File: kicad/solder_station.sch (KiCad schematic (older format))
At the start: 31 parts, among them IC1 ATMEGA328-P, P1 CONN_01X05, P2 CONN_01X02, P3 GX16-8 Plug, P4 UART, Q1 2N7000, Q2 IRF4905, SW1 SPST, U1 LM2596_module, U2 AD8572, U3 EC11, Y1 16MHz

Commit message: [Kicad] Update Schematics. Use local labels.
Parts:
- removed P3: GX16-8 Plug, symbol CONN_01X08
- removed SW1: SPST, symbol SPST
- added D1, D2: D, Diodes_ThroughHole:Diode_DO-35_SOD27_Horizontal_RM10, symbol D
- added P3: Standby, Socket_Strips:Socket_Strip_Straight_1x01, symbol CONN_01X01
- added R10, R11: 1MΩ, Resistors_ThroughHole:Resistor_Horizontal_RM10mm, symbol R
- P1: footprint Pin_Headers:Pin_Header_Straight_1x05 -> Terminal_Blocks:TerminalBlock_Pheonix_MPT-2.54mm_5pol
- P4: footprint Pin_Headers:Pin_Header_Straight_1x03 -> Pin_Headers:Pin_Header_Straight_1x04
- Q2: symbol Q_NMOS_SGD -> Q_PMOS_SGD
- R4: value 1kΩ -> 6.7kΩ
- U3: footprint Buttons_Switches_ThroughHole:KSA_Tactile_SPST -> Pin_Headers:Pin_Header_Straight_1x05
- Y1: footprint Crystals:Crystal_HC51-U_Vertical -> Crystals:Crystal_HC49-U_Vertical
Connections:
- net labels added: Heater_PWM, Temp_sense, Tip
- net labels removed: Button_standby, Heater, RESET, Temp_sens
- wire segments 120 -> 116
- no-connect marks 11 -> 8
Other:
- note added: "Can also use a single Zener diode"
- note added: "Pin 3 and 5 are shorted by connector"
- note removed: "Extern am Addon"
- note removed: "Not part of pcb"
- moved on the sheet: C6, R4

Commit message: [Kicad] Fix bug in schematics (VGS too high). Still not sure if it is okay this way.
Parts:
- added R12: 1kΩ, Resistors_ThroughHole:Resistor_Horizontal_RM10mm, symbol R
- P1: footprint Terminal_Blocks:TerminalBlock_Pheonix_MPT-2.54mm_5pol -> Terminal_Blocks:TerminalBlock_Pheonix_PT-3.5mm_5pol
- P2: footprint Terminal_Blocks:TerminalBlock_Pheonix_MKDS1.5-2pol -> Terminal_Blocks:TerminalBlock_Pheonix_PT-3.5mm_2pol
- P3: footprint Socket_Strips:Socket_Strip_Straight_1x01 -> Pin_Headers:Pin_Header_Straight_1x01
- R5: value 10kΩ -> 1kΩ
- Y1: footprint Crystals:Crystal_HC49-U_Vertical -> Crystals:HC-49V
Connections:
- net GND: now also R12.2; no longer Q1.3 (S)
- new net: Q1.3 (S), R12.1
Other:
- moved on the sheet: R3
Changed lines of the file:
@@
 L GND #PWR06
 U 1 1 566AFDB2
-P 8300 3500
-F 0 "#PWR06" H 8300 3250 50  0001 C CNN
-F 1 "GND" H 8300 3350 50  0000 C CNN
-F 2 "" H 8300 3500 60  0000 C CNN
-F 3 "" H 8300 3500 60  0000 C CNN
-	1    8300 3500
+P 8300 3950
+F 0 "#PWR06" H 8300 3700 50  0001 C CNN
+F 1 "GND" H 8300 3800 50  0000 C CNN
+F 2 "" H 8300 3950 60  0000 C CNN
+F 3 "" H 8300 3950 60  0000 C CNN
+	1    8300 3950
 	1    0    0    -1
 $EndComp
@@
 L R R3
 U 1 1 566AFE19
-P 8100 3400
-F 0 "R3" V 8180 3400 50  0000 C CNN
-F 1 "10kΩ" V 8100 3400 50  0000 C CNN
-F 2 "Resistors_ThroughHole:Resistor_Horizontal_RM10mm" V 8030 3400 30  0001 C CNN
-F 3 "" H 8100 3400 30  0000 C CNN
-	1    8100 3400
+P 8100 3700
+F 0 "R3" V 8180 3700 50  0000 C CNN
+F 1 "10kΩ" V 8100 3700 50  0000 C CNN
+F 2 "Resistors_ThroughHole:Resistor_Horizontal_RM10mm" V 8030 3700 30  0001 C CNN
+F 3 "" H 8100 3700 30  0000 C CNN
+	1    8100 3700
 	0    -1   -1   0
 $EndComp
@@
 P 8300 1950
 F 0 "R5" V 8380 1950 50  0000 C CNN
-F 1 "10kΩ" V 8300 1950 50  0000 C CNN
+F 1 "1kΩ" V 8300 1950 50  0000 C CNN
 F 2 "Resistors_ThroughHole:Resistor_Horizontal_RM10mm" V 8230 1950 30  0001 C CNN
 F 3 "" H 8300 1950 30  0000 C CNN
@@
 F 0 "P2" H 7600 1350 50  0000 C CNN
 F 1 "CONN_01X02" V 7700 1200 50  0000 C CNN
-F 2 "Terminal_Blocks:TerminalBlock_Pheonix_MKDS1.5-2pol" H 7600 1200 60  0001 C CNN
+F 2 "Terminal_Blocks:TerminalBlock_Pheonix_PT-3.5mm_2pol" H 7600 1200 60  0001 C CNN
 F 3 "" H 7600 1200 60  0000 C CNN
 	1    7600 1200
@@
 F 0 "P1" H 10500 1000 50  0000 C CNN
 F 1 "CONN_01X05" V 10600 700 50  0000 C CNN
-F 2 "Terminal_Blocks:TerminalBlock_Pheonix_MPT-2.54mm_5pol" H 10500 700 60  0001 C CNN
+F 2 "Terminal_Blocks:TerminalBlock_Pheonix_PT-3.5mm_5pol" H 10500 700 60  0001 C CNN
 F 3 "" H 10500 700 60  0000 C CNN
 	1    10500 700
@@
 F 0 "Y1" V 5800 3400 50  0000 C CNN
 F 1 "16MHz" H 5800 3100 50  0000 C CNN
-F 2 "Crystals:Crystal_HC49-U_Vertical" H 5800 3250 60  0001 C CNN
+F 2 "Crystals:HC-49V" H 5800 3250 60  0001 C CNN
 F 3 "" H 5800 3250 60  0000 C CNN
 	1    5800 3250
@@
 F 0 "P3" H 6050 3900 50  0000 C CNN
 F 1 "Standby" V 6150 3800 50  0000 C CNN
-F 2 "Socket_Strips:Socket_Strip_Straight_1x01" H 6050 3800 60  0001 C CNN
+F 2 "Pin_Headers:Pin_Header_Straight_1x01" H 6050 3800 60  0001 C CNN
 F 3 "" H 6050 3800 60  0000 C CNN
 	1    6050 3800
@@
 	7800 3050 8000 3050
 Wire Wire Line
-	8300 3250 8300 3500
-Wire Wire Line
-	7950 3400 7950 3050
+	7950 3050 7950 3700
 Connection ~ 7950 3050
-Wire Wire Line
-	8250 3400 8300 3400
-Connection ~ 8300 3400
 Wire Wire Line
 	9100 1550 9100 2050
@@
 Text Label 7050 4900 0    60   ~ 0
 Heater+
+$Comp
+L R R12
+U 1 1 56A90FE1
+P 8300 3450
+F 0 "R12" V 8380 3450 50  0000 C CNN
+F 1 "1kΩ" V 8300 3450 50  0000 C CNN
+F 2 "Resistors_ThroughHole:Resistor_Horizontal_RM10mm" V 8230 3450 30  0001 C CNN
+F 3 "" H 8300 3450 30  0000 C CNN
+	1    8300 3450
+	1    0    0    -1
+$EndComp
+Wire Wire Line
+	8300 3300 8300 3250
+Wire Wire Line
+	8300 3600 8300 3950
+Wire Wire Line
+	8250 3700 8300 3700
+Connection ~ 8300 3700
 $EndSCHEMATC

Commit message: [Kicad] Update schematics. Using ad8551.
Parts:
- added C9: CP, Capacitors_ThroughHole:C_Radial_D5_L11_P2.5, symbol CP
- Q2: symbol Q_PMOS_SGD -> Q_PMOS_GDS
- R1: value 100kΩ -> 10kΩ
- R10: value 1MΩ -> 300kΩ
- R6: value 100Ω -> 1kΩ
- R7: value 50kΩ -> 100kΩ
- U2: value AD8572 -> AD8551; symbol LM358 -> TL071
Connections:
- net +24V: now also C9.1
- net AVcc: now also U2.7 (V+); no longer U2.8 (V+)
- net Button_push: now also IC1.16 ((PCINT2/OC1B/~SS~)PB2); no longer IC1.17 ((PCINT3/OC2A/MOSI)PB3)
- net GND: now also Q1.1 (D), C9.2; no longer R12.2
- net Heater+: now also Q2.2 (D); no longer Q2.1 (S)
- net Rotary_B: now also IC1.17 ((PCINT3/OC2A/MOSI)PB3); no longer IC1.18 ((PCINT4/MISO)PB4)
- net at Q1.3 (S): now also R12.2; no longer R12.1
- net at R7.1, R8.2: now also U2.6; no longer U2.1
- new net: Q2.1 (G), R12.1, R5.2
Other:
- note removed: "Can also use a single Zener diode"
- note removed: "Wert muss noch ermittelt werden"
- moved on the sheet: P2, R12
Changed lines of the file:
@@
 P 5900 4350
 F 0 "R1" V 6000 4400 50  0000 C CNN
-F 1 "100kΩ" V 5800 4350 50  0000 C CNN
+F 1 "10kΩ" V 5800 4350 50  0000 C CNN
 F 2 "Resistors_ThroughHole:Resistor_Horizontal_RM10mm" V 5830 4350 30  0001 C CNN
 F 3 "" H 5900 4350 30  0000 C CNN
@@
 	1    0    0    -1
 $EndComp
-NoConn ~ 4950 2850
 $Comp
 L Q_NMOS_DGS Q1
@@
 F 3 "" H 8200 3050 60  0000 C CNN
 	1    8200 3050
-	1    0    0    -1
+	1    0    0    1
 $EndComp
 $Comp
@@
 $EndComp
 $Comp
-L Q_PMOS_SGD Q2
+L Q_PMOS_GDS Q2
 U 1 1 566B0176
 P 9000 2250
@@
 F 3 "" H 9000 2250 60  0000 C CNN
 	1    9000 2250
-	1    0    0    -1
+	1    0    0    1
 $EndComp
 $Comp
@@
 P 9700 5650
 F 0 "R6" V 9780 5650 50  0000 C CNN
-F 1 "100Ω" V 9700 5650 50  0000 C CNN
+F 1 "1kΩ" V 9700 5650 50  0000 C CNN
 F 2 "Resistors_ThroughHole:Resistor_Horizontal_RM10mm" V 9630 5650 30  0001 C CNN
 F 3 "" H 9700 5650 30  0000 C CNN
@@
 P 9700 5200
 F 0 "R7" V 9780 5200 50  0000 C CNN
-F 1 "50kΩ" V 9700 5200 50  0000 C CNN
+F 1 "100kΩ" V 9700 5200 50  0000 C CNN
 F 2 "Resistors_ThroughHole:Resistor_Horizontal_RM10mm" V 9630 5200 30  0001 C CNN
 F 3 "" H 9700 5200 30  0000 C CNN
@@
 	1    0    0    -1
 $EndComp
-Text Notes 9250 6100 0    39   ~ 0
-Wert muss noch ermittelt werden
 Text GLabel 2800 2750 1    60   Output ~ 0
 AVcc
@@
 L CONN_01X02 P2
 U 1 1 566DD427
-P 7600 1200
-F 0 "P2" H 7600 1350 50  0000 C CNN
-F 1 "CONN_01X02" V 7700 1200 50  0000 C CNN
-F 2 "Terminal_Blocks:TerminalBlock_Pheonix_PT-3.5mm_2pol" H 7600 1200 60  0001 C CNN
-F 3 "" H 7600 1200 60  0000 C CNN
-	1    7600 1200
+P 7600 1350
+F 0 "P2" H 7600 1500 50  0000 C CNN
+F 1 "CONN_01X02" V 7700 1350 50  0000 C CNN
+F 2 "Terminal_Blocks:TerminalBlock_Pheonix_PT-3.5mm_2pol" H 7600 1350 60  0001 C CNN
+F 3 "" H 7600 1350 60  0000 C CNN
+	1    7600 1350
 	0    1    1    0
 $EndComp
@@
 L +24V #PWR024
 U 1 1 566DD4CA
-P 7650 900
-F 0 "#PWR024" H 7650 750 50  0001 C CNN
-F 1 "+24V" H 7650 1040 50  0000 C CNN
-F 2 "" H 7650 900 60  0000 C CNN
-F 3 "" H 7650 900 60  0000 C CNN
-	1    7650 900
+P 7850 800
+F 0 "#PWR024" H 7850 650 50  0001 C CNN
+F 1 "+24V" H 7850 940 50  0000 C CNN
+F 2 "" H 7850 800 60  0000 C CNN
+F 3 "" H 7850 800 60  0000 C CNN
+	1    7850 800
 	1    0    0    -1
 $EndComp
@@
 L GND #PWR025
 U 1 1 566DD545
-P 7550 800
-F 0 "#PWR025" H 7550 550 50  0001 C CNN
-F 1 "GND" H 7550 650 50  0000 C CNN
-F 2 "" H 7550 800 60  0000 C CNN
-F 3 "" H 7550 800 60  0000 C CNN
-	1    7550 800
+P 7300 750
+F 0 "#PWR025" H 7300 500 50  0001 C CNN
+F 1 "GND" H 7300 600 50  0000 C CNN
+F 2 "" H 7300 750 60  0000 C CNN
+F 3 "" H 7300 750 60  0000 C CNN
+	1    7300 750
 	-1   0    0    1
 $EndComp
 $Comp
-L LM358 U2
+L TL071 U2
 U 1 1 566D9405
 P 9150 5000
 F 0 "U2" H 9100 5200 60  0000 L CNN
-F 1 "AD8572" H 9100 4750 60  0000 L CNN
+F 1 "AD8551" H 9100 4750 60  0000 L CNN
 F 2 "Housings_SOIC:SOIC-8_3.9x4.9mm_Pitch1.27mm" H 9150 5000 60  0001 C CNN
 F 3 "" H 9150 5000 60  0000 C CNN
@@
 P 7450 4400
 F 0 "R10" V 7530 4400 50  0000 C CNN
-F 1 "1MΩ" V 7450 4400 50  0000 C CNN
+F 1 "300kΩ" V 7450 4400 50  0000 C CNN
 F 2 "Resistors_ThroughHole:Resistor_Horizontal_RM10mm" V 7380 4400 30  0001 C CNN
 F 3 "" H 7450 4400 30  0000 C CNN
@@
 Text GLabel 7450 4000 1    60   Input ~ 0
 AVcc
-Text Notes 7500 5750 0    60   ~ 0
-Can also use a single Zener diode
 $Comp
 L R R11
@@
 	8800 2250 8300 2250
 Wire Wire Line
-	8300 2100 8300 2850
-Wire Wire Line
 	8300 1800 9100 1800
 Connection ~ 9100 1800
@@
 Connection ~ 9050 5950
 Wire Wire Line
-	7550 800  7550 1000
-Wire Wire Line
-	7650 900  7650 1000
-Wire Wire Line
 	2900 1000 3250 1000
 Wire Wire Line
@@
 	6400 4450 6400 4600
 Wire Wire Line
-	4950 2950 5550 2950
+	4950 2850 5550 2850
 Wire Wire Line
 	4950 3150 5400 3150
@@
 Text Label 6400 4600 1    60   ~ 0
 DTR
-Text Label 5550 2950 2    60   ~ 0
+Text Label 5550 2850 2    60   ~ 0
 Button_push
 Text Label 6650 1650 2    60   ~ 0
 Button_push
-Text Label 5400 3050 2    60   ~ 0
+Text Label 5400 2950 2    60   ~ 0
 Rotary_B
 Wire Wire Line
-	5400 3050 4950 3050
+	5400 2950 4950 2950
 Text Label 5400 3150 2    60   ~ 0
 Rotary_A
@@
 L R R12
 U 1 1 56A90FE1
-P 8300 3450
-F 0 "R12" V 8380 3450 50  0000 C CNN
-F 1 "1kΩ" V 8300 3450 50  0000 C CNN
-F 2 "Resistors_ThroughHole:Resistor_Horizontal_RM10mm" V 8230 3450 30  0001 C CNN
-F 3 "" H 8300 3450 30  0000 C CNN
-	1    8300 3450
-	1    0    0    -1
-$EndComp
-Wire Wire Line
-	8300 3300 8300 3250
-Wire Wire Line
-	8300 3600 8300 3950
+P 8300 2600
+F 0 "R12" V 8400 2600 50  0000 C CNN
+F 1 "1kΩ" V 8300 2600 50  0000 C CNN
+F 2 "Resistors_ThroughHole:Resistor_Horizontal_RM10mm" V 8230 2600 30  0001 C CNN
+F 3 "" H 8300 2600 30  0000 C CNN
+	1    8300 2600
+	1    0    0    -1
+$EndComp
+Wire Wire Line
+	8300 3250 8300 3950
 Wire Wire Line
 	8250 3700 8300 3700
 Connection ~ 8300 3700
+Wire Wire Line
+	8300 2100 8300 2450
+Wire Wire Line
+	8300 2750 8300 2850
+NoConn ~ 4950 3050
+$Comp
+L CP C9
+U 1 1 56B3C013
+P 7600 800
+F 0 "C9" H 7625 900 50  0000 L CNN
+F 1 "CP" H 7625 700 50  0000 L CNN
+F 2 "Capacitors_ThroughHole:C_Radial_D5_L11_P2.5" H 7638 650 30  0001 C CNN
+F 3 "" H 7600 800 60  0000 C CNN
+	1    7600 800
+	0    1    1    0
+$EndComp
+Wire Wire Line
+	7650 1150 7800 1150
+Wire Wire Line
+	7750 800  7850 800
+Wire Wire Line
+	7450 800  7300 800
+Wire Wire Line
+	7300 800  7300 750
+Wire Wire Line
+	7400 800  7400 1150
+Wire Wire Line
+	7400 1150 7550 1150
+Connection ~ 7400 800
+Wire Wire Line
+	7800 1150 7800 800
+Connection ~ 7800 800
 $EndSCHEMATC

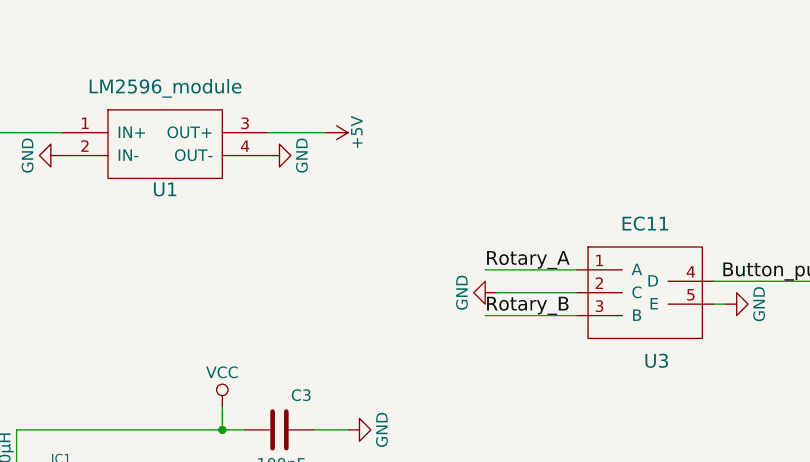
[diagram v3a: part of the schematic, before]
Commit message: [Kicad] Update schematics. Use smd capacitors. Add big capacitor for 24V input. Add first approach to fix #1 (still incomplete. Needs testing).
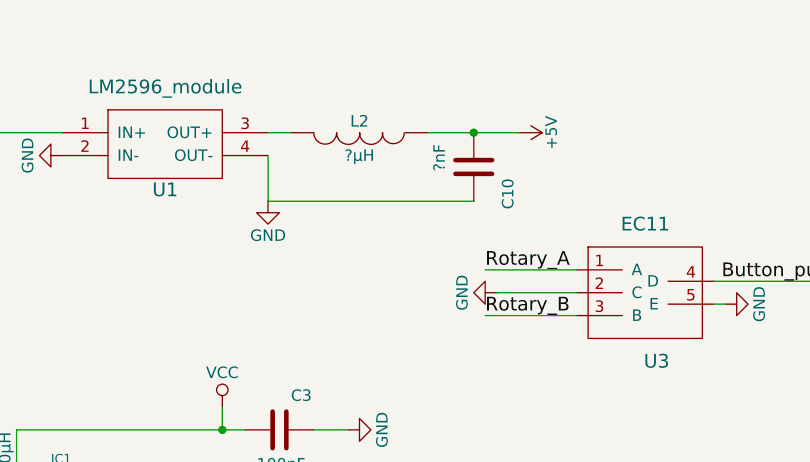
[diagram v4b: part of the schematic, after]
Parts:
- added C10: ?nF, Capacitors_SMD:C_0603_HandSoldering, symbol C
- added L2: ?µH, Choke_Axial_ThroughHole:Choke_Horizontal_RM10mm, symbol INDUCTOR
- C1, C2, C3, C8: footprint Capacitors_ThroughHole:C_Disc_D3_P2.5 -> Capacitors_SMD:C_0603_HandSoldering
- C9: footprint Capacitors_ThroughHole:C_Radial_D5_L11_P2.5 -> Capacitors_ThroughHole:C_Radial_D13_L21_P5
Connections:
- net +5V: now also C10.2, L2.1; no longer U1.3 (OUT+)
- net GND: now also C10.1
- new net: L2.2, U1.3 (OUT+)
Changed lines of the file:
@@
 F 0 "C2" V 2600 3300 50  0000 L CNN
 F 1 "100nF" V 2700 3100 50  0000 L CNN
-F 2 "Capacitors_ThroughHole:C_Disc_D3_P2.5" H 2588 3100 30  0001 C CNN
+F 2 "Capacitors_SMD:C_0603_HandSoldering" H 2588 3100 30  0001 C CNN
 F 3 "" H 2550 3250 60  0000 C CNN
 	1    2550 3250
@@
 F 0 "C1" V 2600 2800 50  0000 L CNN
 F 1 "100nF" V 2700 2550 50  0000 L CNN
-F 2 "Capacitors_ThroughHole:C_Disc_D3_P2.5" H 2588 2600 30  0001 C CNN
+F 2 "Capacitors_SMD:C_0603_HandSoldering" H 2588 2600 30  0001 C CNN
 F 3 "" H 2550 2750 60  0000 C CNN
 	1    2550 2750
@@
 F 0 "C3" V 4050 2350 50  0000 L CNN
 F 1 "100nF" V 4350 2200 50  0000 L CNN
-F 2 "Capacitors_ThroughHole:C_Disc_D3_P2.5" H 4238 2150 30  0001 C CNN
+F 2 "Capacitors_SMD:C_0603_HandSoldering" H 4238 2150 30  0001 C CNN
 F 3 "" H 4200 2300 60  0000 C CNN
 	1    4200 2300
@@
 L GND #PWR026
 U 1 1 56874984
-P 4150 1100
-F 0 "#PWR026" H 4150 850 50  0001 C CNN
-F 1 "GND" H 4150 950 50  0000 C CNN
-F 2 "" H 4150 1100 60  0000 C CNN
-F 3 "" H 4150 1100 60  0000 C CNN
-	1    4150 1100
-	0    -1   -1   0
+P 4150 1300
+F 0 "#PWR026" H 4150 1050 50  0001 C CNN
+F 1 "GND" H 4150 1150 50  0000 C CNN
+F 2 "" H 4150 1300 60  0000 C CNN
+F 3 "" H 4150 1300 60  0000 C CNN
+	1    4150 1300
+	1    0    0    -1
 $EndComp
 $Comp
@@
 L +5V #PWR029
 U 1 1 56874C19
-P 4400 1000
-F 0 "#PWR029" H 4400 850 50  0001 C CNN
-F 1 "+5V" H 4400 1140 50  0000 C CNN
-F 2 "" H 4400 1000 60  0000 C CNN
-F 3 "" H 4400 1000 60  0000 C CNN
-	1    4400 1000
+P 5250 1000
+F 0 "#PWR029" H 5250 850 50  0001 C CNN
+F 1 "+5V" H 5250 1140 50  0000 C CNN
+F 2 "" H 5250 1000 60  0000 C CNN
+F 3 "" H 5250 1000 60  0000 C CNN
+	1    5250 1000
 	0    1    1    0
 $EndComp
@@
 F 0 "C8" V 6250 4350 50  0000 L CNN
 F 1 "100nF" V 6550 4200 50  0000 L CNN
-F 2 "Capacitors_ThroughHole:C_Disc_D3_P2.5" H 6438 4150 30  0001 C CNN
+F 2 "Capacitors_SMD:C_0603_HandSoldering" H 6438 4150 30  0001 C CNN
 F 3 "" H 6400 4300 60  0000 C CNN
 	1    6400 4300
@@
 Wire Wire Line
 	2900 1000 3250 1000
-Wire Wire Line
-	4150 1000 4400 1000
 Wire Wire Line
 	4950 4450 5250 4450
@@
 F 0 "C9" H 7625 900 50  0000 L CNN
 F 1 "CP" H 7625 700 50  0000 L CNN
-F 2 "Capacitors_ThroughHole:C_Radial_D5_L11_P2.5" H 7638 650 30  0001 C CNN
+F 2 "Capacitors_ThroughHole:C_Radial_D13_L21_P5" H 7638 650 30  0001 C CNN
 F 3 "" H 7600 800 60  0000 C CNN
 	1    7600 800
@@
 	7800 1150 7800 800
 Connection ~ 7800 800
+$Comp
+L C C10
+U 1 1 56CCC257
+P 5050 1150
+F 0 "C10" V 4900 1200 50  0000 L CNN
+F 1 "?nF" V 5200 1050 50  0000 L CNN
+F 2 "Capacitors_SMD:C_0603_HandSoldering" H 5088 1000 30  0001 C CNN
+F 3 "" H 5050 1150 60  0000 C CNN
+	1    5050 1150
+	-1   0    0    1
+$EndComp
+Wire Wire Line
+	4250 1000 4150 1000
+Wire Wire Line
+	5050 1300 4150 1300
+Wire Wire Line
+	4150 1300 4150 1100
+Wire Wire Line
+	4850 1000 5250 1000
+Connection ~ 5050 1000
+$Comp
+L INDUCTOR L2
+U 1 1 56CCC88E
+P 4550 1000
+F 0 "L2" V 4500 1000 50  0000 C CNN
+F 1 "?µH" V 4650 1000 50  0000 C CNN
+F 2 "Choke_Axial_ThroughHole:Choke_Horizontal_RM10mm" H 4550 1000 60  0001 C CNN
+F 3 "" H 4550 1000 60  0000 C CNN
+	1    4550 1000
+	0    1    1    0
+$EndComp
 $EndSCHEMATC
